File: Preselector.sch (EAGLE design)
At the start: 185 parts, among them IC4 TPS7A8101DRB, IC58 LMZ31707RVQ, Q2 FDV303N, X1 0733660061, X10 0733660061, X11 0733660061, X12 0733660061, X13 0733660061, X14 0733660061, X15 0733660061, X16 0733660061, X17 0733660061, X18 0733660061, X19 0733660061, X2 0733660061, X20 0733660061, X21 0733660061, X22 0733660061, X23 0733660061, X24 0733660061, X25 0733660061, X26 0733660061, X27 0733660061, X28 0733660061, X29 0733660061, X3 0733660061, X30 0733660061, X31 0733660061, X32 0733660061, X4 0733660061, X5 0733660061, X6 0733660061, X7 0733660061, X8 0733660061, X9 0733660061

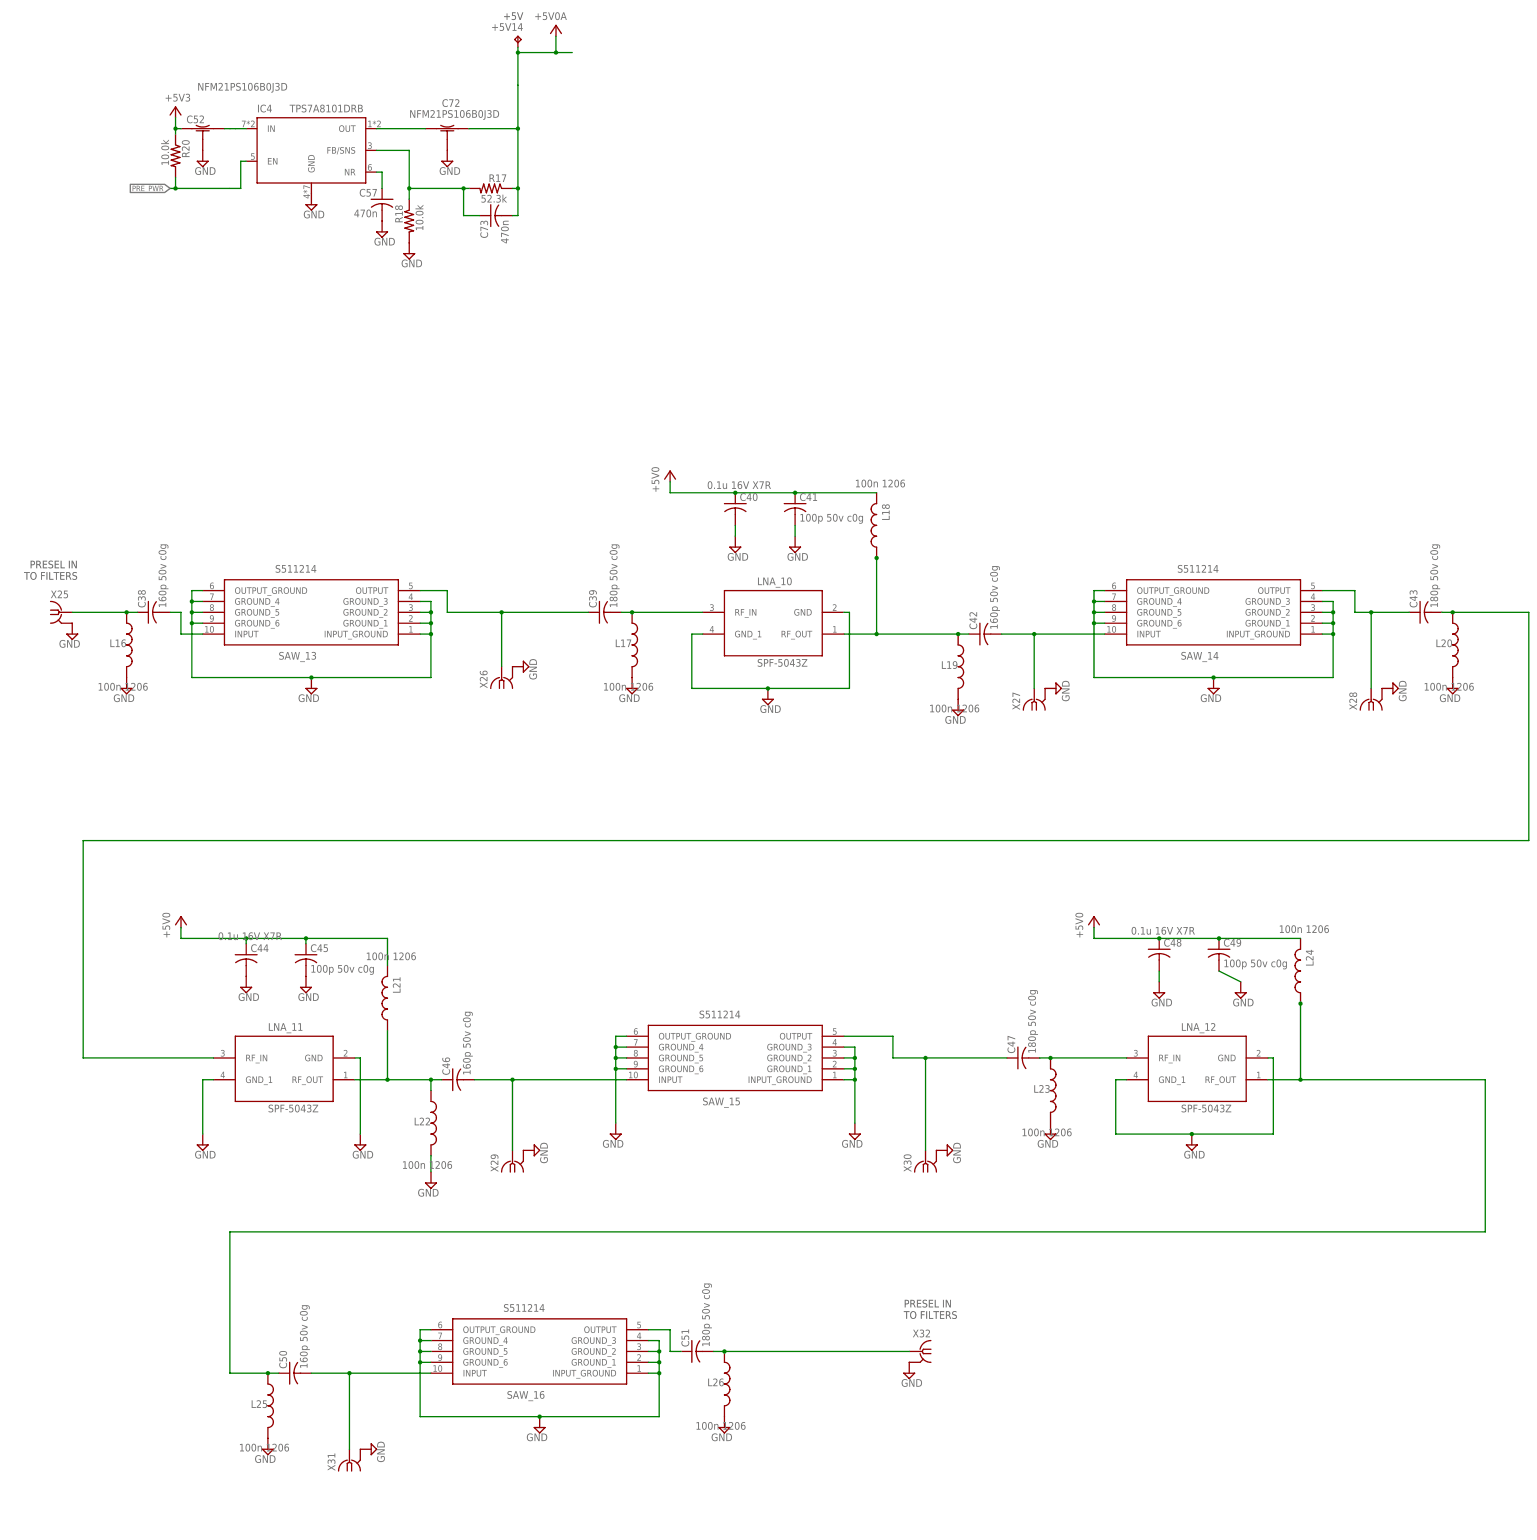
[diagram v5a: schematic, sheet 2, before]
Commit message: Added LDO's to schematic, will add to board shortly.
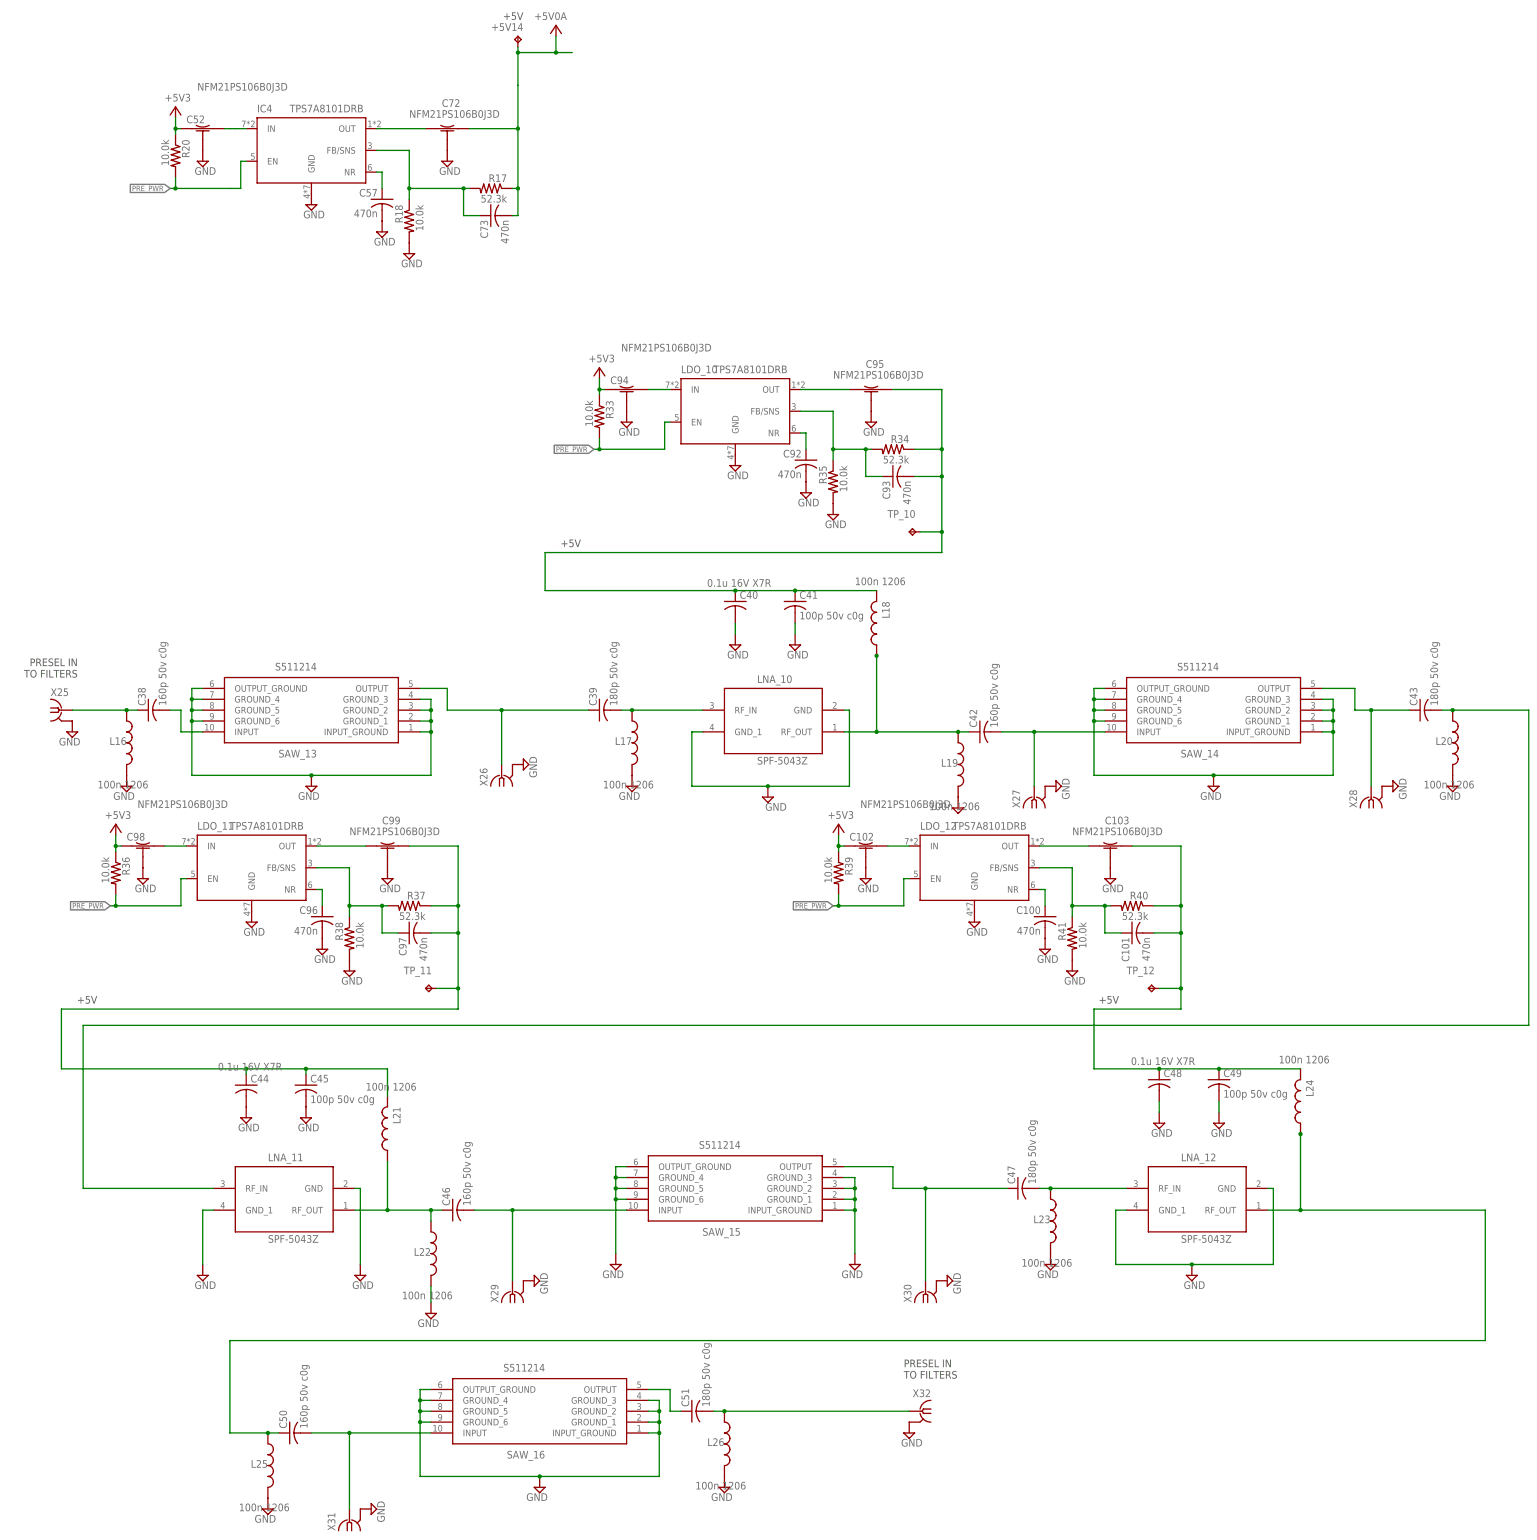
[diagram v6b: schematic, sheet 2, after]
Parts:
- added C100, C101, C62, C63, C66, C67, C70, C71, C76, C77, C80, C81, C84, C85, C88, C89, C92, C93, C96, C97: 470n, rcl:C-USC0402K
- added C102, C103, C64, C65, C68, C69, C74, C75, C78, C79, C82, C83, C86, C87, C90, C91, C94, C95, C98, C99: NFM21PS106B0J3D, DEEP EDDY:NFM21PS
- added LDO_10, LDO_11, LDO_12, LDO_3, LDO_4, LDO_5, LDO_6, LDO_7, LDO_8, LDO_9: TPS7A8101DRB, DEEP EDDY:TPS7A8101DRB
- added R10, R11, R14, R15, R19, R21, R23, R24, R26, R27, R29, R30, R32, R33, R35, R36, R38, R39, R41, R8: 10.0k, rcl:R-US_R0603
- added R12, R16, R22, R25, R28, R31, R34, R37, R40, R9: 52.3k, rcl:R-US_R0603
- added TP_10, TP_11, TP_12, TP_3, TP_4, TP_5, TP_6, TP_7, TP_8, TP_9: TPTP20SQ, testpad:TPTP20SQ
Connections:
- removed net +5V0: C10.1, C11.1, C15.1, C16.1, C19.1, C20.1, C23.1, C24.1, C27.1, C28.1, C31.1, C32.1, C35.1, C36.1, C40.1, C41.1, C44.1, C45.1, C48.1, C49.1, C6.1, C7.1, L10.2, L11.2, L12.1, L13.2, L14.2, L15.2, L18.2, L21.2, L24.2, L4.2, L7.1
- removed net LDO_1_5V1: C59.2, C61.OUT, R6.1, TP_2.TP
- new net LDO_10_5V: C40.1, C41.1, C93.2, C95.OUT, L18.2, R34.1, TP_10.TP
- new net LDO_11_5V: C44.1, C45.1, C97.2, C99.OUT, L21.2, R37.1, TP_11.TP
- new net LDO_12_5V: C101.2, C103.OUT, C48.1, C49.1, L24.2, R40.1, TP_12.TP
- new net LDO_2_5V: C59.2, C6.1, C61.OUT, C7.1, L4.2, R6.1, TP_2.TP
- new net LDO_3_5V: C10.1, C11.1, C63.2, C65.OUT, L7.1, R9.1, TP_3.TP
- new net LDO_4_5V: C15.1, C16.1, C67.2, C69.OUT, L10.2, R12.1, TP_4.TP
- new net LDO_5_5V: C19.1, C20.1, C71.2, C75.OUT, L11.2, R16.1, TP_5.TP
- new net LDO_6_5V: C23.1, C24.1, C77.2, C79.OUT, L12.1, R22.1, TP_6.TP
- new net LDO_7_5V: C27.1, C28.1, C81.2, C83.OUT, L13.2, R25.1, TP_7.TP
- new net LDO_8_5V: C31.1, C32.1, C85.2, C87.OUT, L14.2, R28.1, TP_8.TP
- new net LDO_9_5V: C35.1, C36.1, C89.2, C91.OUT, L15.2, R31.1, TP_9.TP
- new net N$20: C63.1, LDO_3.FB/SNS, R10.1, R9.2
- new net N$22: C62.1, LDO_3.NR
- new net N$24: C64.OUT, LDO_3.IN
- new net N$25: C65.IN, LDO_3.OUT
- new net N$27: C67.1, LDO_4.FB/SNS, R12.2, R14.1
- new net N$28: C66.1, LDO_4.NR
- new net N$30: C68.OUT, LDO_4.IN
- new net N$33: C69.IN, LDO_4.OUT
- new net N$34: C71.1, LDO_5.FB/SNS, R16.2, R19.1
- new net N$36: C70.1, LDO_5.NR
- new net N$38: C74.OUT, LDO_5.IN
- new net N$39: C75.IN, LDO_5.OUT
- new net N$40: C81.1, LDO_7.FB/SNS, R25.2, R26.1
- new net N$41: C77.1, LDO_6.FB/SNS, R22.2, R23.1
- new net N$42: C76.1, LDO_6.NR
- new net N$43: C78.OUT, LDO_6.IN
- new net N$45: C79.IN, LDO_6.OUT
- new net N$46: C80.1, LDO_7.NR
- new net N$47: C82.OUT, LDO_7.IN
- new net N$48: C83.IN, LDO_7.OUT
- new net N$49: C85.1, LDO_8.FB/SNS, R28.2, R29.1
- new net N$50: C84.1, LDO_8.NR
- new net N$51: C86.OUT, LDO_8.IN
- new net N$52: C87.IN, LDO_8.OUT
- new net N$53: C89.1, LDO_9.FB/SNS, R31.2, R32.1
- new net N$54: C88.1, LDO_9.NR
- new net N$56: C90.OUT, LDO_9.IN
- new net N$57: C91.IN, LDO_9.OUT
- new net N$61: C93.1, LDO_10.FB/SNS, R34.2, R35.1
- new net N$62: C92.1, LDO_10.NR
- new net N$63: C94.OUT, LDO_10.IN
- new net N$64: C95.IN, LDO_10.OUT
- new net N$66: C97.1, LDO_11.FB/SNS, R37.2, R38.1
- new net N$67: C96.1, LDO_11.NR
- new net N$68: C98.OUT, LDO_11.IN
- new net N$69: C99.IN, LDO_11.OUT
- new net N$70: C101.1, LDO_12.FB/SNS, R40.2, R41.1
- new net N$71: C100.1, LDO_12.NR
- new net N$72: C102.OUT, LDO_12.IN
- new net N$73: C103.IN, LDO_12.OUT
- net +5V3: now also C102.IN, C64.IN, C68.IN, C74.IN, C78.IN, C82.IN, C86.IN, C90.IN, C94.IN, C98.IN, R11.1, R15.1, R21.1, R24.1, R27.1, R30.1, R33.1, R36.1, R39.1, R8.1
- net GND: now also C100.2, C102.GND, C103.GND, C62.2, C64.GND, C65.GND, C66.2, C68.GND, C69.GND, C70.2, C74.GND, C75.GND, C76.2, C78.GND, C79.GND, C80.2, C82.GND, C83.GND, C84.2, C86.GND, C87.GND, C88.2, C90.GND, C91.GND, C92.2, C94.GND, C95.GND, C96.2, C98.GND, C99.GND, LDO_10.GND, LDO_11.GND, LDO_12.GND, LDO_3.GND, LDO_4.GND, LDO_5.GND, LDO_6.GND, LDO_7.GND, LDO_8.GND, LDO_9.GND, R10.2, R14.2, R19.2, R23.2, R26.2, R29.2, R32.2, R35.2, R38.2, R41.2
- net PRE_PWR: now also LDO_10.EN, LDO_11.EN, LDO_12.EN, LDO_3.EN, LDO_4.EN, LDO_5.EN, LDO_6.EN, LDO_7.EN, LDO_8.EN, LDO_9.EN, R11.2, R15.2, R21.2, R24.2, R27.2, R30.2, R33.2, R36.2, R39.2, R8.2
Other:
- moved on the sheet: C10, C11, C12, C13, C38, C39, C40, C41, C42, C43, C44, C45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
